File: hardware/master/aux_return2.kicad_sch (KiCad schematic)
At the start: 108 parts, among them J301 RETURN 2 L/MONO, J302 RETURN 2 R, J303 GAIN: fitted -6 dB (PRO), ope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, SW301 RETURN 2 MUTE (latching), SW302 RETURN 2 DUCK (latching), SW303 RETURN 2 COMP (latching), U301 TL072, U302 NE5532, U303 SSI2162, U304 NE5532, U305 NE5532, U306 OPA2171, U307 TL072, U308 DG413DY, U309 DG413DY

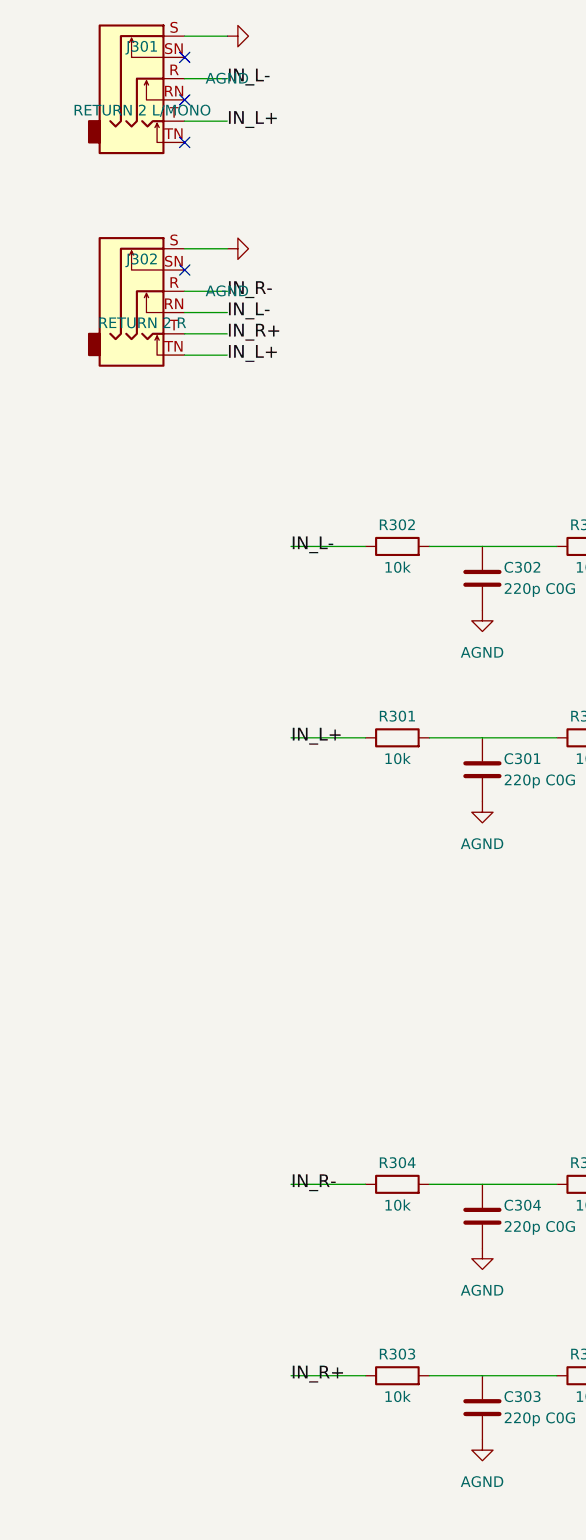
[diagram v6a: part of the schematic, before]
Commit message: Master: rear jacks on two 26-pin row-board ribbons (decision 163)
J603 (AUX sends sheet) carries main outs and both AUX sends to the
output row board; J903 (Power sheet) brings the AUX returns, SC EXT
and the ground-lift switch (pins 25/26) from the input row board.
Pairs with a ground between them; row boards hold only jacks, header
and SW901. Netlist checks 0 problems, ERC 0/0.

Co-Authored-By: Claude Opus 5.5 <noreply@anthropic.com>
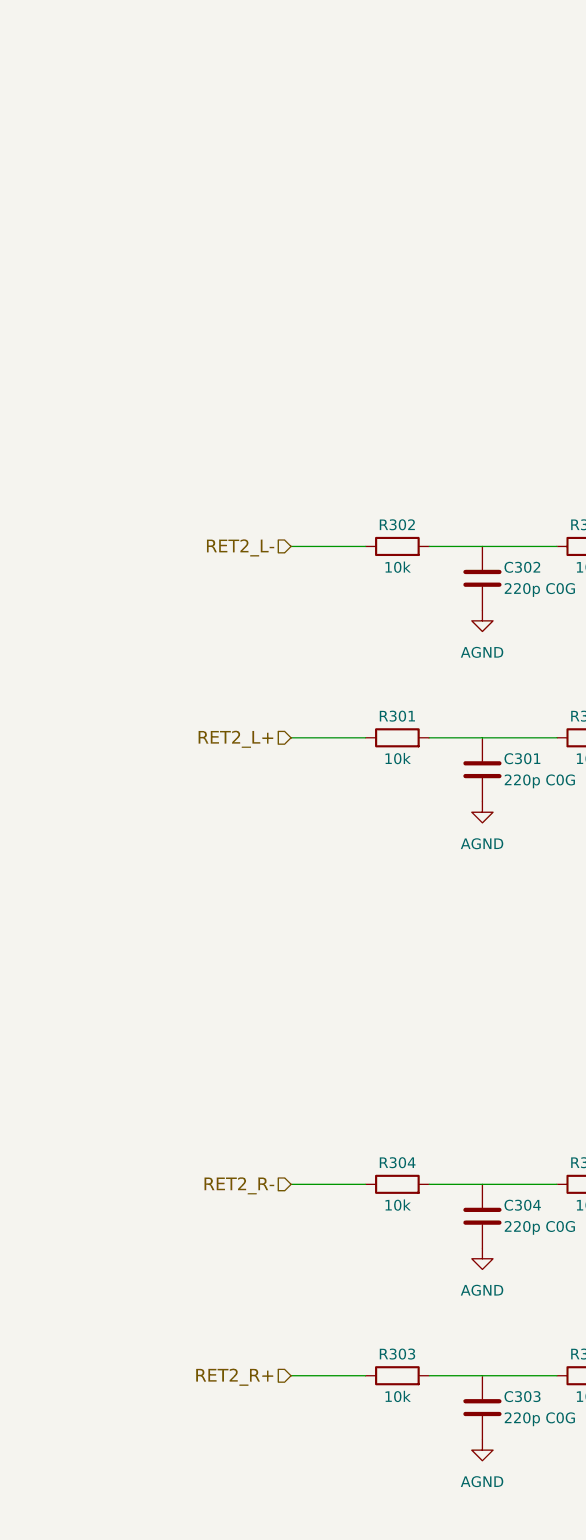
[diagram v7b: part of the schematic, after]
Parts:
- removed J301: RETURN 2 L/MONO, syntsamix:Jack_6.35mm_Rean_NYS216_Horizontal, symbol Connector_Audio:AudioJack3_Switch
- removed J302: RETURN 2 R, syntsamix:Jack_6.35mm_Rean_NYS216_Horizontal, symbol Connector_Audio:AudioJack3_Switch
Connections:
- net IN_L+ renamed RET2_L+
- net IN_L- renamed RET2_L-
- net IN_R+ renamed RET2_R+
- net IN_R- renamed RET2_R-
- no-connect marks 10 -> 6

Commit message: Master: back-to-back coupling pairs, ten NE5532 to TL072, Wakefield heatsinks, onsemi TO-220 regulators (decisions 172-174)
Co-Authored-By: Claude Opus 5.5 <noreply@anthropic.com>
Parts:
- removed C305, C306, C309, C310: 10u bipolar, Capacitor_SMD:C_Elec_6.3x5.4, symbol Device:C
- removed U302, U304, U305: NE5532, Package_SO:SOIC-8_3.9x4.9mm_P1.27mm, symbol Amplifier_Operational:NE5532
- added C305, C306, C309, C310, C334, C335, C336, C337: 10u 35V, Capacitor_SMD:CP_Elec_5x5.4, symbol Device:C_Polarized
- added U302, U304, U305: TL072, Package_SO:SOIC-8_3.9x4.9mm_P1.27mm, symbol Amplifier_Operational:TL072
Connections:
- net +15V: now also U302.8 (V+), U304.8 (V+), U305.8 (V+)
- net -15V: now also U302.4 (V-), U304.4 (V-), U305.4 (V-)
- net AGND: now also U302.3 (+), U302.5 (+), U304.3 (+), U304.5 (+), U305.3 (+), U305.5 (+)
- net R_RET: now also C310.1, U302.7
- net at R346.2, U301.1: now also C305.1
- net at C314.1, R316.1, U303.7 (IOUT2): now also U304.6 (-)
- net at C314.2, R316.2, R318.1: now also U304.7
- net at C308.1, R306.2, R308.1: now also U302.6 (-)
- net at R350.2, U301.7: now also C306.1
- net at R306.1: now also C335.1
- net at R318.2, R320.1: now also U305.6 (-)
- net at R320.2, R335.1: now also U305.7
- net at C307.2, J303.2 (Pin_2), R309.2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: now also C309.1, U302.1
- net at R319.2, R334.1: now also U305.1
- net at R311.1: now also C336.1
- net at C307.1, R305.2, R307.1: now also U302.2 (-)
- net at C313.1, R315.1, U303.4 (IOUT1): now also U304.2 (-)
- net at R317.2, R319.1: now also U305.2 (-)
- net at C313.2, R315.2, R317.1: now also U304.1
- net at R312.1: now also C337.1
- net at R305.1: now also C334.1
- new net: C309.2, C336.2
- new net: C306.2, C335.2
- new net: C310.2, C337.2
- new net: C305.2, C334.2
